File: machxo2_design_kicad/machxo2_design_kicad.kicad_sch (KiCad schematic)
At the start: 0 parts

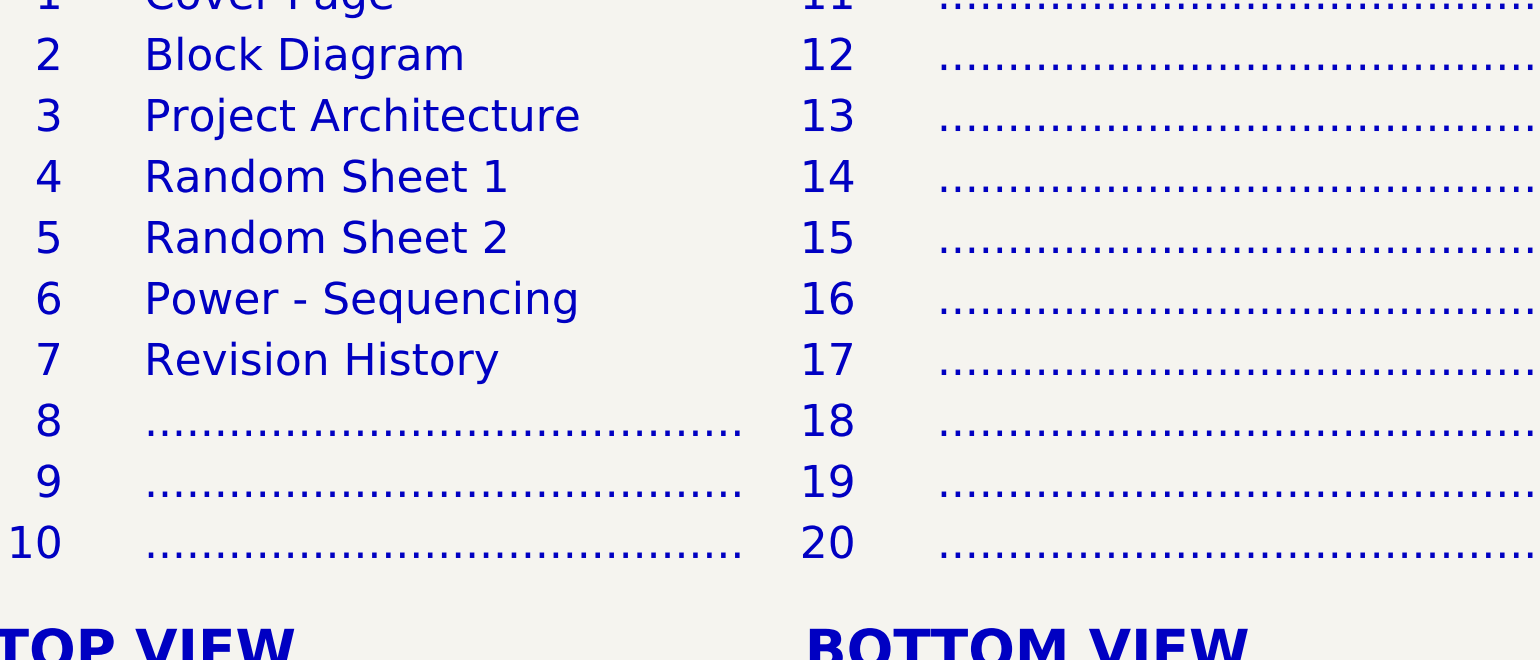
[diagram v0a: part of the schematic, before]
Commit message: Prelimary schematic done. Need to create BOM and review.
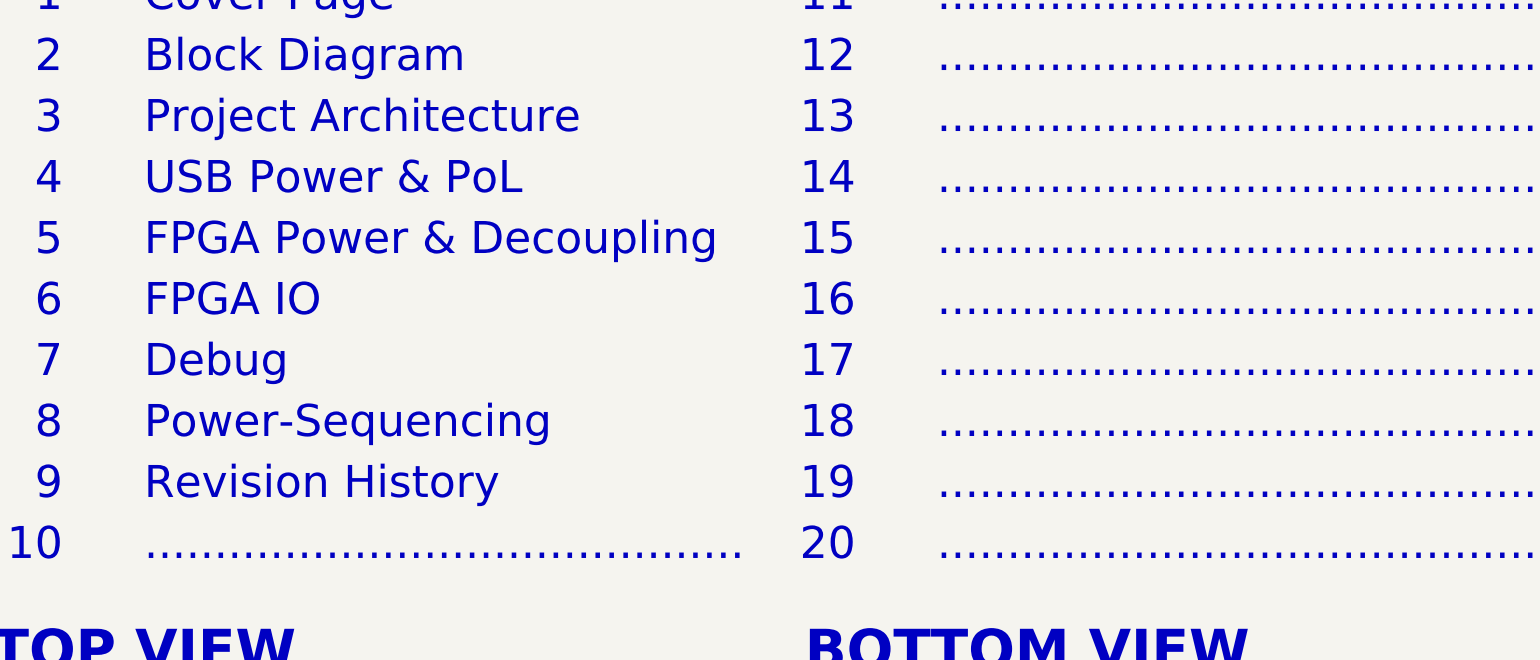
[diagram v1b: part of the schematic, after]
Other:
- note added: "Debug"
- note added: "FPGA IO"
- note added: "FPGA Power & Decoupling"
- note added: "Power-Sequencing"
- note added: "USB Power & PoL"
- note removed: "Power - Sequencing"
- note removed: "Random Sheet 1"
- note removed: "Random Sheet 2"
